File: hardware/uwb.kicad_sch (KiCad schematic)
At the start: 0 parts

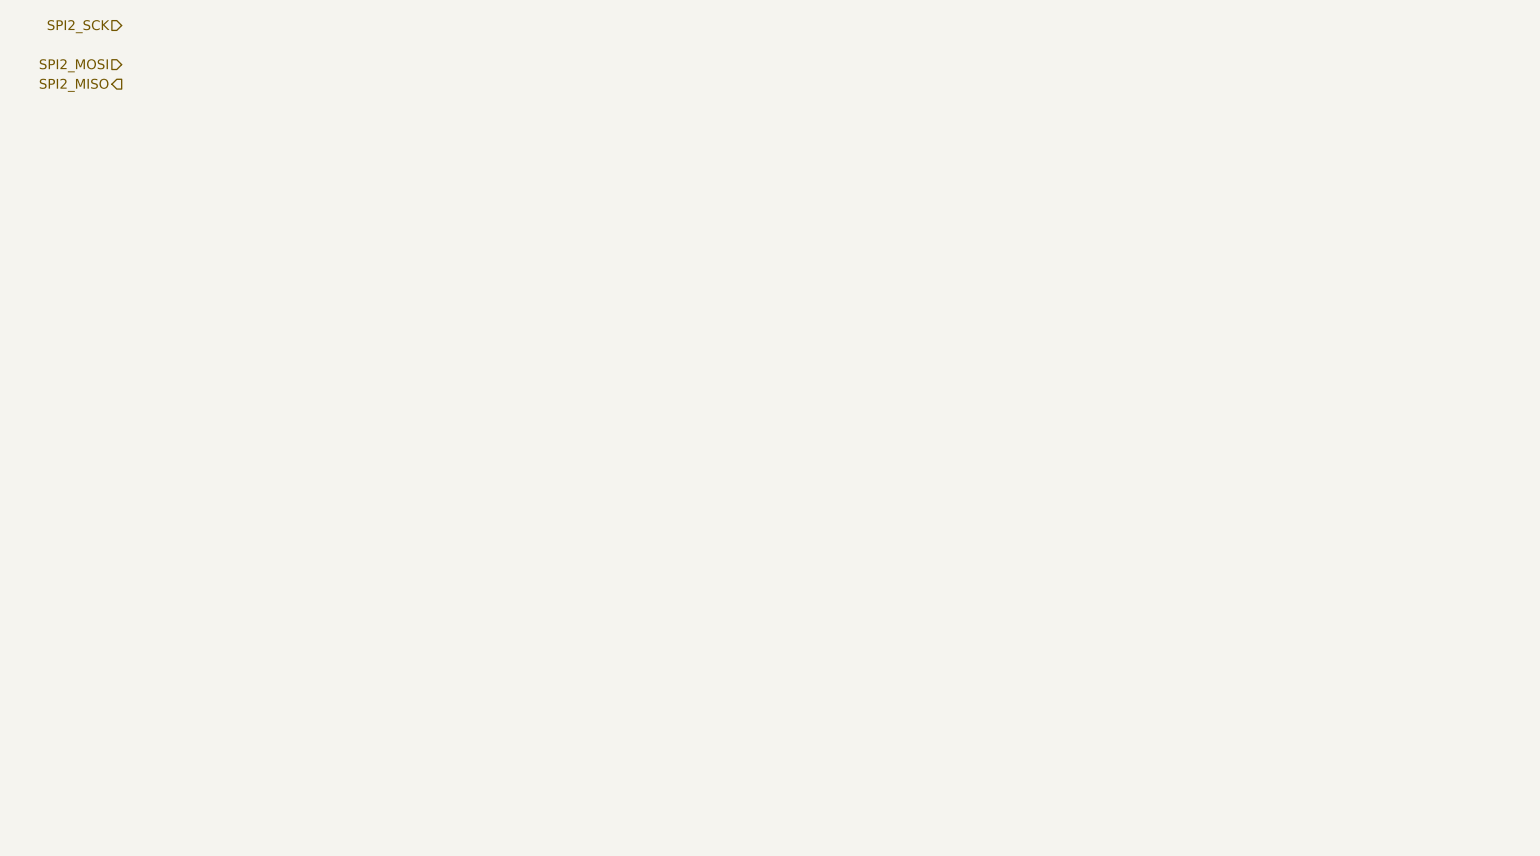
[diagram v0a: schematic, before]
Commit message: feat(kicad): Added several open sourced footprint libraries, finished schematic design for nrf, uwb, tof, flash, motors and added all reference material to refs folder
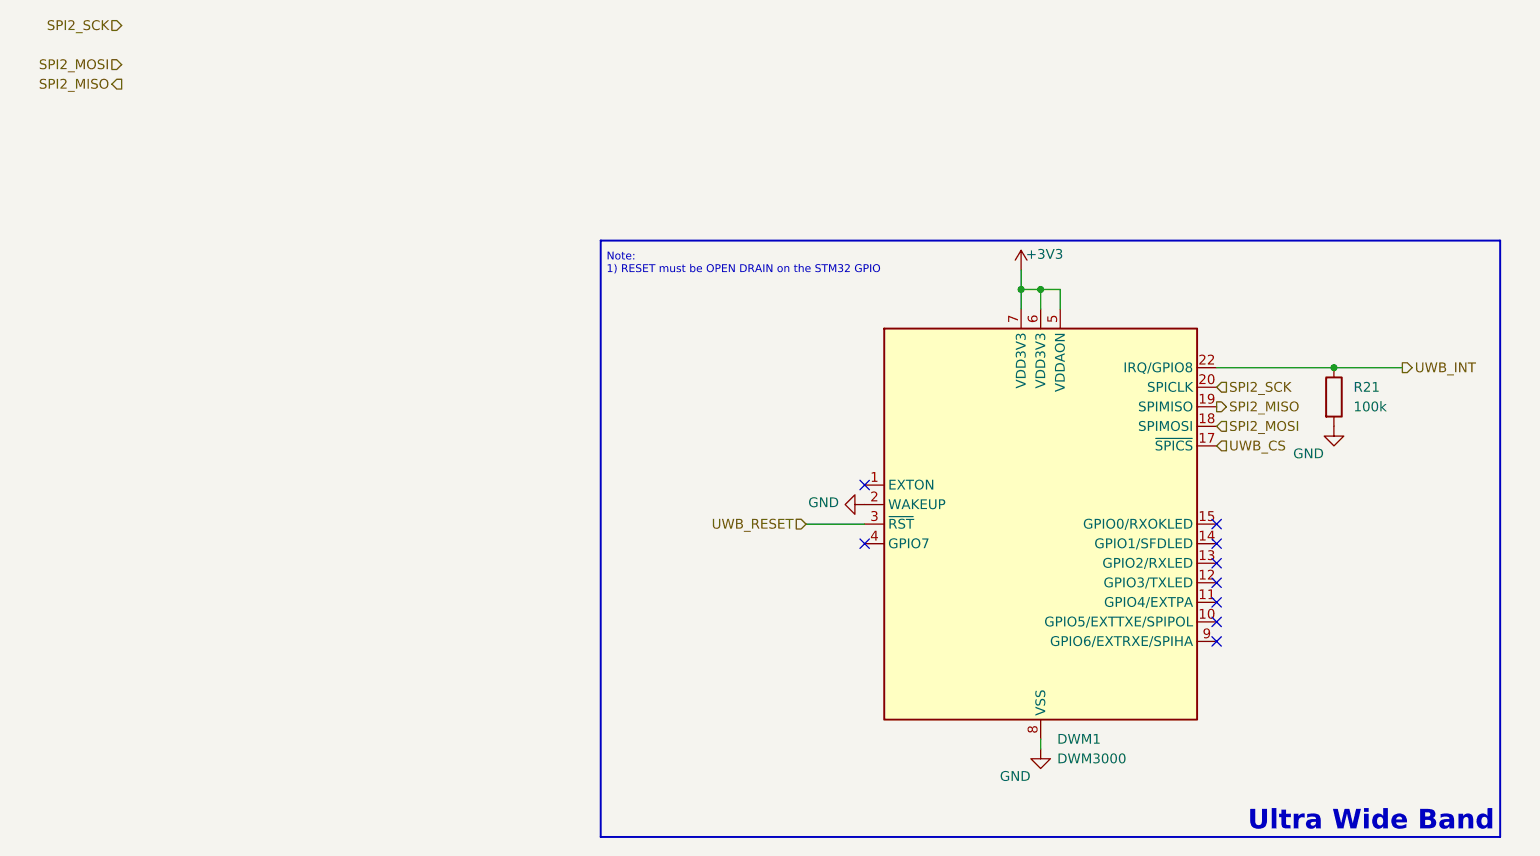
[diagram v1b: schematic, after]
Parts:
- added DWM1: DWM3000, RF_Module:DWM1000, symbol RF_Module:DWM3000
- added R21: 100k, symbol Device:R
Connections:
- net SPI2_MISO: now also DWM1.19 (SPIMISO)
- net SPI2_MOSI: now also DWM1.18 (SPIMOSI)
- net SPI2_SCK: now also DWM1.20 (SPICLK)
- new net +3V3: DWM1.5 (VDDAON), DWM1.6 (VDD3V3), DWM1.7 (VDD3V3)
- new net GND: DWM1.16 (VSS), DWM1.2 (WAKEUP), DWM1.21 (VSS), DWM1.23 (VSS), DWM1.24 (VSS), DWM1.8 (VSS), R21.2
- new net UWB_CS: DWM1.17 (~{SPICS})
- new net UWB_INT: DWM1.22 (IRQ/GPIO8), R21.1
- new net UWB_RESET: DWM1.3 (~{RST})
- no-connect marks 0 -> 9
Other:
- note added: "Note: 1) RESET must be OPEN DRAIN on the STM32 GPIO"
- note added: "Ultra Wide Band"
